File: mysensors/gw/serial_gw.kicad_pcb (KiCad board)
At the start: 2 copper layers, 44.5 x 19.8 mm, 69 parts, among them CON1 AVR-ISP-6, IC1 ATMEGA328P-MU, P1 USB_A, P2 ANTENNA, SW1 RESET, U1 TXB0104, U2 MCP1703A-3302, U3 CP2102, U4 RFM69W, U5 ATSHA204A, X1 16MHz

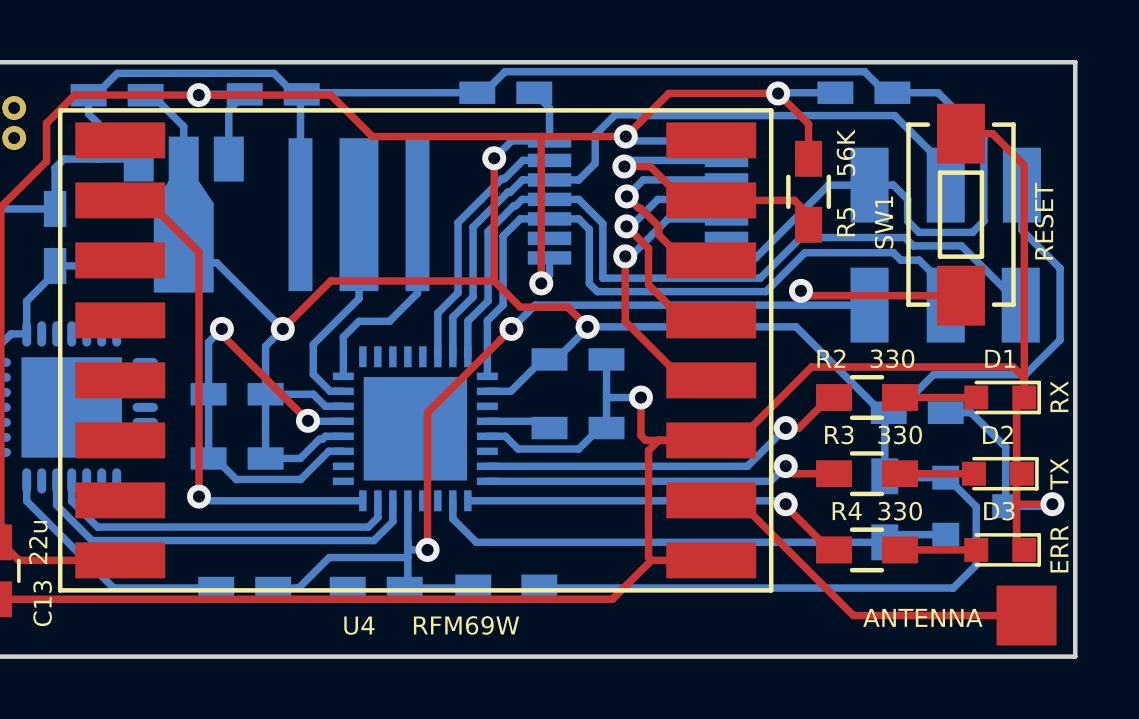
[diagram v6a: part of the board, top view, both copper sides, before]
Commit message: [mysensors_gw] pcb design - fixed ceramic resonator pins
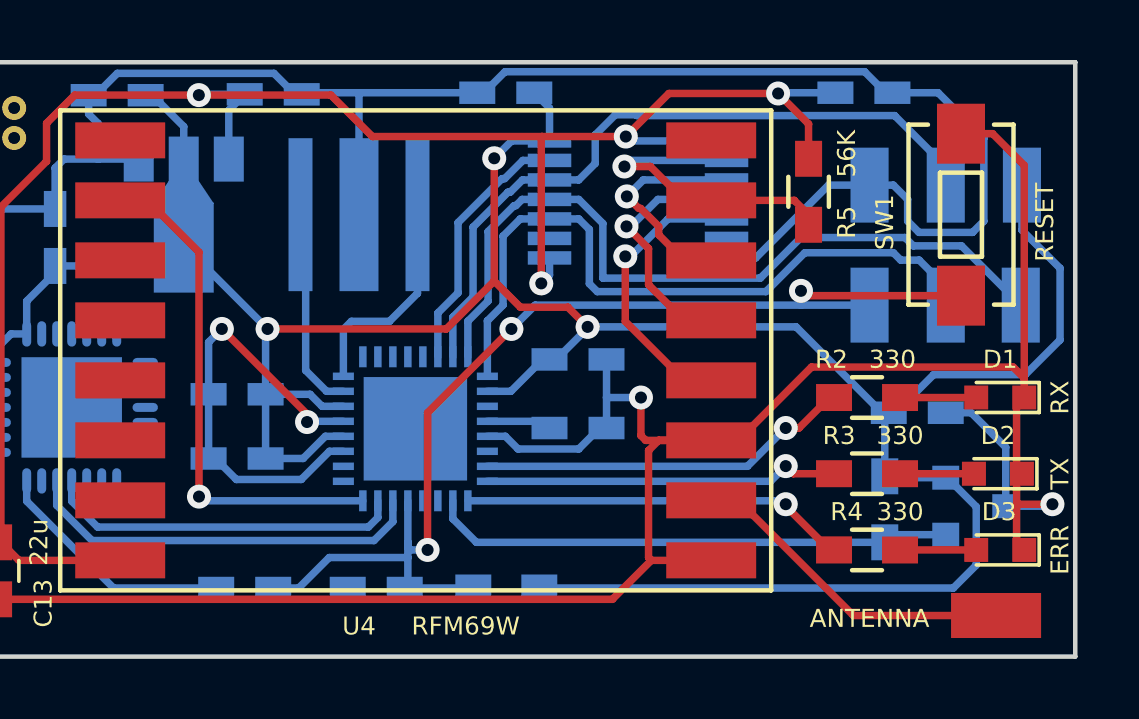
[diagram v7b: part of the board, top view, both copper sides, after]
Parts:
- moved P2 1.02 mm to (112.8, 92.2)
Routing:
- net Net-(P2-Pad1): track 12.1 -> 11.1 mm
- net Net-(IC1-Pad7): track 7.19 -> 6.36 mm
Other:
- board text added: "Rev. 0.2"
- board text removed: "Rev. 0.1"

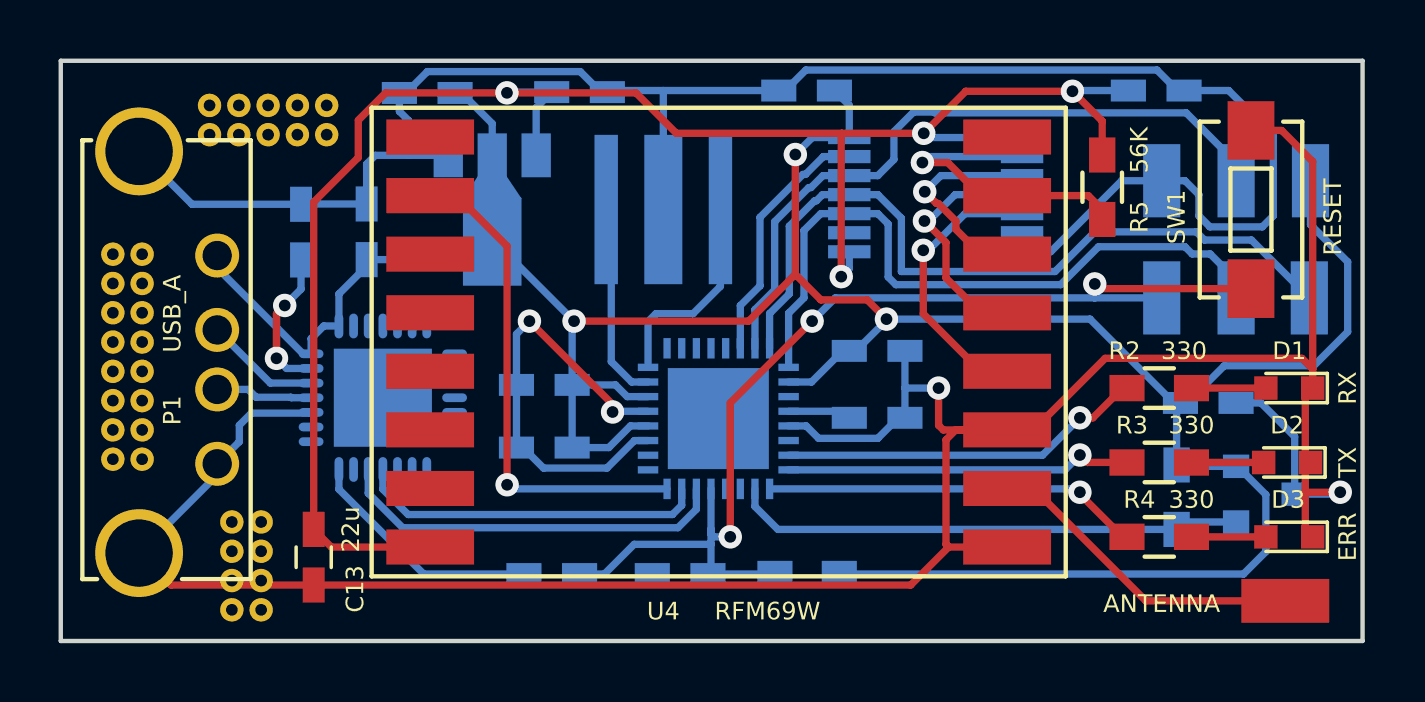
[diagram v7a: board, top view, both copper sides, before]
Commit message: [mysensors_gw] pcb design - estetic touches
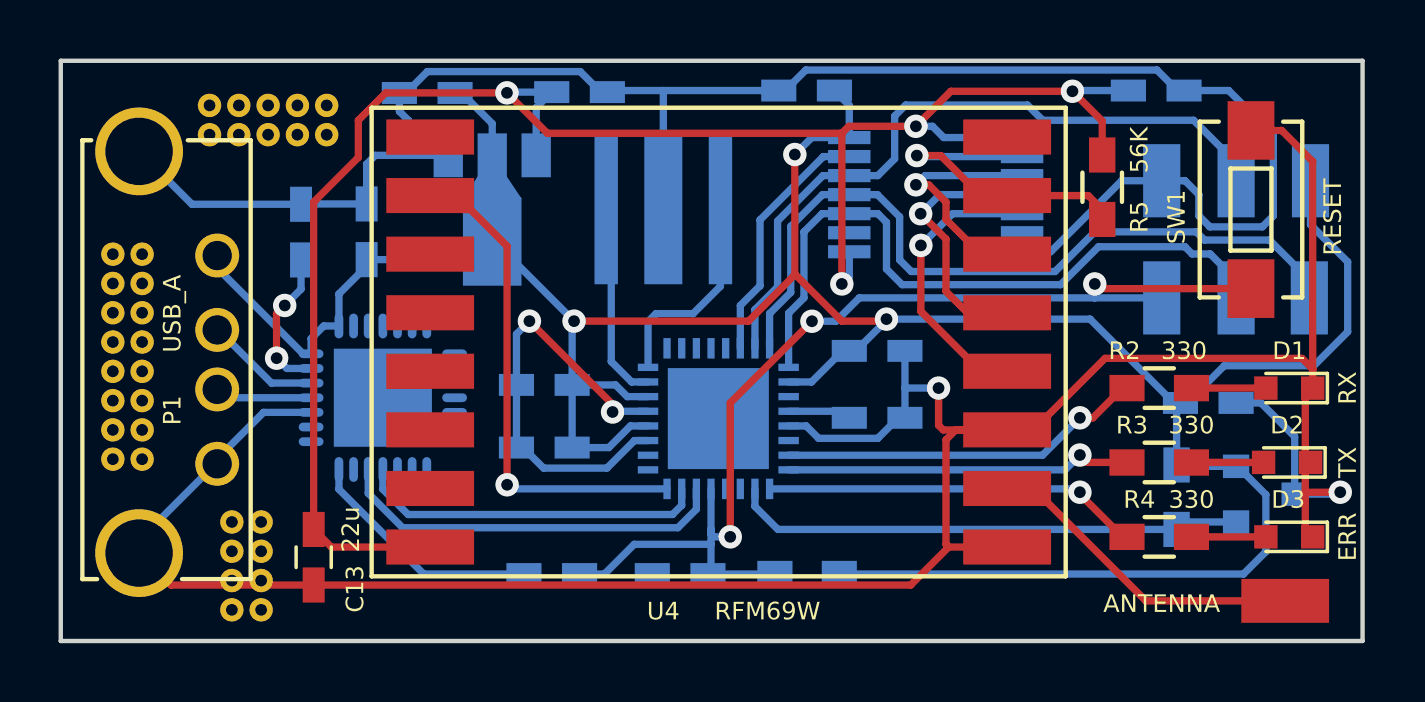
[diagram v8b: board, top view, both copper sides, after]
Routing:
- net +3V3: track 62.5 -> 63.4 mm
- net Net-(U1-Pad3): track 7.41 -> 8.20 mm
- net Net-(U1-Pad4): track 8.54 -> 9.13 mm
